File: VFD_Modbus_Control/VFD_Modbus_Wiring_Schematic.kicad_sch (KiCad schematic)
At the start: 11 parts

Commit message: Added the wiring to tie the grounds for the 5V PSU and the G540 PSU
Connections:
- net at Relay1. (NO): now also VFD1. (X6/Y1_FO)
- net at VFD1. (X6/Y1_FO): now also SPINDLE1. (RED); no longer Relay1. (NO)
- net at G1.10 (DISABLE_INPUT_(E-STOP)), G1.12 (POWER_SUPPLY_GND), PSU2. (+): now also PSU1. (+), Relay1. (NO), UC300ETH1. (DB25)
- new net: D1.1 (K), PSU1. (+), Relay1. (NO), UC300ETH1. (DB25)
- new net: Relay1. (NO), VFD1. (X6/Y1_FO)
- new net: RS485USB1. (+), VFD1. (X6/Y1_FO)
- new net: G1.7 (VFD_GROUND), PSU3. (L), SPINDLE1. (RED), VFD1. (X6/Y1_FO)
- new net: PSU3. (L), PUMP1. (L), VFD1. (X6/Y1_FO)
- new net: SPINDLE1. (RED), VFD1. (X6/Y1_FO) (x2)
- now unconnected: PSU1. (+), PSU1. (+)
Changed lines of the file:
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@@
+	)
+	(junction
+		(at 217.17 63.5)
+		(diameter 0)
+		(color 0 0 0 0)
 	)
 	(junction
@@
 	)
 	(junction
+		(at 217.17 49.53)
+		(diameter 0)
+		(color 0 0 0 0)
+	)
+	(junction
 		(at 227.33 52.07)
 		(diameter 0)
@@
 	(wire
 		(pts
-			(xy 200.66 49.53) (xy 270.51 49.53)
+			(xy 200.66 49.53) (xy 217.17 49.53)
 		)
 		(stroke
@@
 	(wire
 		(pts
+			(xy 217.17 49.53) (xy 217.17 63.5)
+		)
+		(stroke
+			(width 0)
+			(type default)
+		)
+	)
+	(wire
+		(pts
 			(xy 52.07 54.61) (xy 100.33 54.61)
 		)
@@
 		)
 		(stroke
+			(width 0)
+			(type default)
+		)
+	)
+	(wire
+		(pts
+			(xy 217.17 49.53) (xy 270.51 49.53)
+		)
+		(stroke

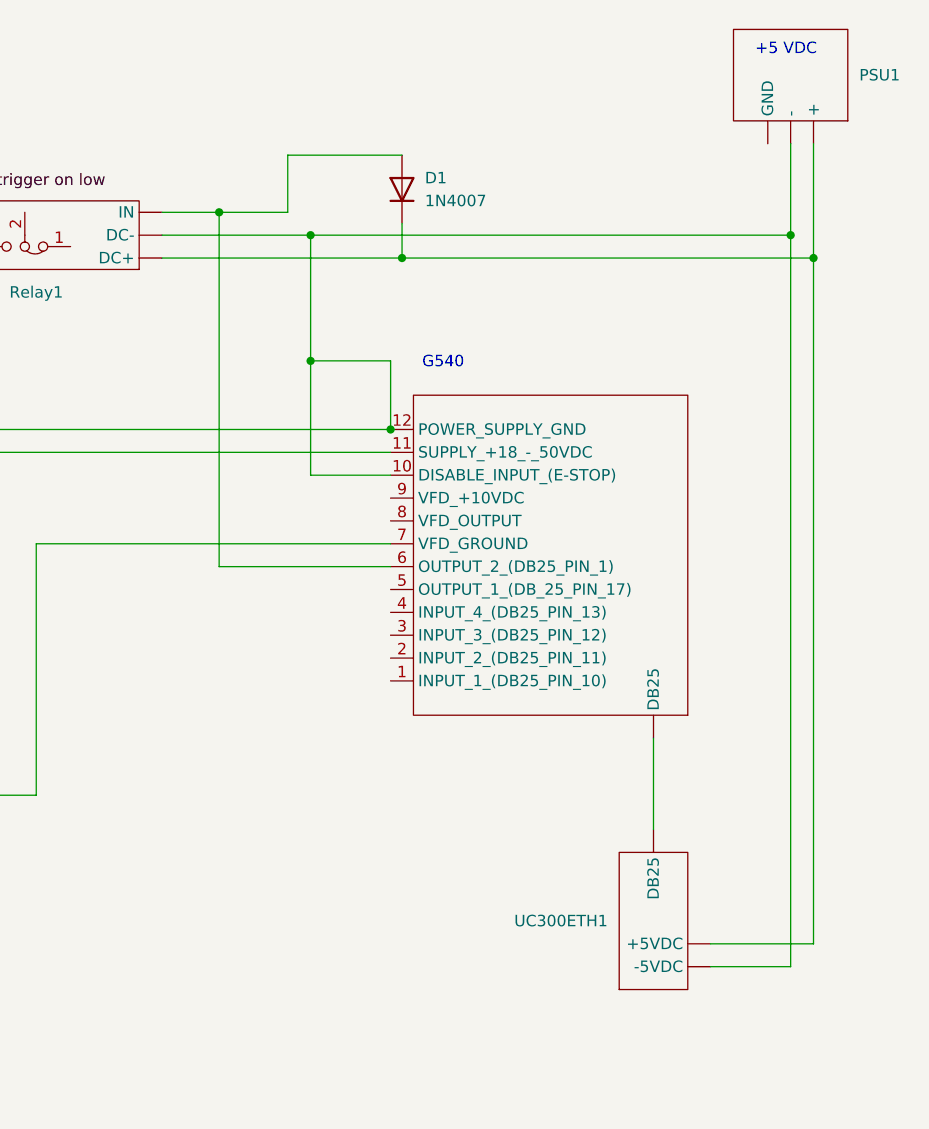
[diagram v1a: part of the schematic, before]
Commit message: Got voltage control working using two relays.
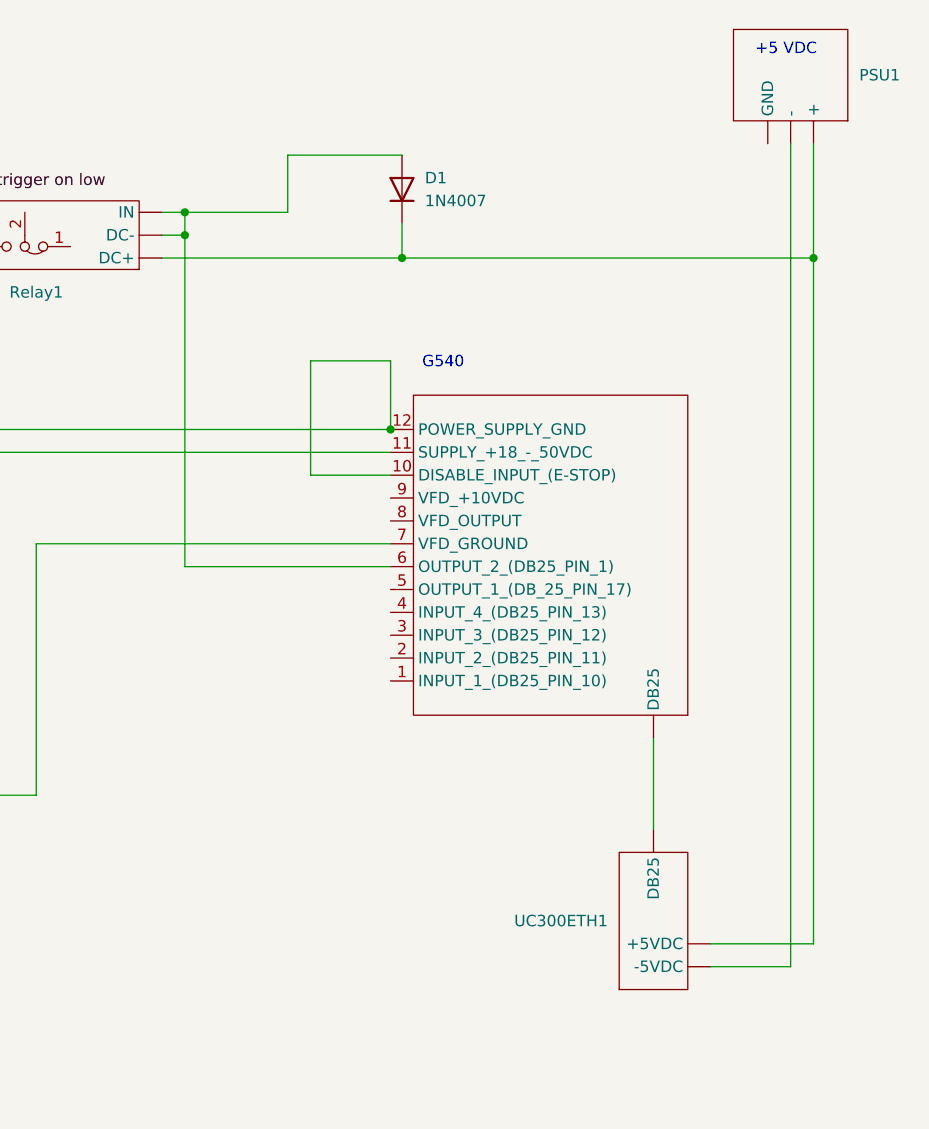
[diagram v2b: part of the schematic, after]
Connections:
- net at Relay1. (NO): now also VFD1. (X6/Y1_FO)
- net at VFD1. (X6/Y1_FO): now also SPINDLE1. (RED); no longer Relay1. (NO)
- new net: D1.1 (K), PSU1. (+), Relay1. (NO), UC300ETH1. (DB25)
- new net: Relay1. (NO), VFD1. (X6/Y1_FO)
- new net: RS485USB1. (+), VFD1. (X6/Y1_FO)
- new net: G1.10 (DISABLE_INPUT_(E-STOP)), G1.12 (POWER_SUPPLY_GND), PSU2. (+)
- new net: G1.7 (VFD_GROUND), PSU3. (L), SPINDLE1. (RED), VFD1. (X6/Y1_FO)
- new net: PSU3. (L), PUMP1. (L), VFD1. (X6/Y1_FO)
- new net: PSU1. (+), UC300ETH1. (DB25)
- new net: SPINDLE1. (RED), VFD1. (X6/Y1_FO) (x2)
- now unconnected: PSU1. (+), PSU1. (+), PSU2. (+)
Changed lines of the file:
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@@
-	)
-	(junction
-		(at 207.01 46.99)
-		(diameter 0)
-		(color 0 0 0 0)
-	)
-	(junction
-		(at 217.17 63.5)
-		(diameter 0)
-		(color 0 0 0 0)
 	)
 	(junction
@@
 	)
 	(junction
-		(at 270.51 49.53)
-		(diameter 0)
-		(color 0 0 0 0)
-	)
-	(junction
-		(at 217.17 49.53)
+		(at 203.2 49.53)
 		(diameter 0)
 		(color 0 0 0 0)
@@
 	)
 	(junction
+		(at 203.2 46.99)
+		(diameter 0)
+		(color 0 0 0 0)
+	)
+	(junction
 		(at 46.99 111.76)
 		(diameter 0)
@@
 	(wire
 		(pts
-			(xy 200.66 49.53) (xy 217.17 49.53)
-		)
-		(stroke
-			(width 0)
-			(type default)
-		)
-	)
-	(wire
-		(pts
 			(xy 20.32 143.51) (xy 95.25 143.51)
 		)
@@
 	(wire
 		(pts
-			(xy 270.51 39.37) (xy 270.51 49.53)
+			(xy 270.51 39.37) (xy 270.51 130.81)
 		)
 		(stroke
@@
 	(wire
 		(pts
-			(xy 217.17 49.53) (xy 217.17 63.5)
-		)
-		(stroke
-			(width 0)
-			(type default)
-		)
-	)
-	(wire
-		(pts
 			(xy 52.07 54.61) (xy 100.33 54.61)
 		)
@@
 	(wire
 		(pts
-			(xy 270.51 49.53) (xy 270.51 130.81)
-		)
-		(stroke
-			(width 0)
-			(type default)
-		)
-	)
-	(wire
-		(pts
 			(xy 78.74 39.37) (xy 78.74 46.99)
 		)
@@
 	(wire
 		(pts
-			(xy 217.17 49.53) (xy 270.51 49.53)
-		)
-		(stroke
-			(width 0)
-			(type default)
-		)
-	)
-	(wire
-		(pts
 			(xy 72.39 176.53) (xy 72.39 168.91)
 		)
@@
 	(wire
 		(pts
+			(xy 203.2 49.53) (xy 203.2 46.99)
+		)
+		(stroke
+			(width 0)
+			(type default)
+		)
+	)
+	(wire
+		(pts
+			(xy 203.2 46.99) (xy 200.66 46.99)
+		)
+		(stroke
+			(width 0)
+			(type default)
+		)
+	)
+	(wire
+		(pts
 			(xy 172.72 49.53) (xy 109.22 49.53)
 		)
@@
 	(wire
 		(pts
-			(xy 207.01 46.99) (xy 200.66 46.99)
-		)
-		(stroke
-			(width 0)
-			(type default)
-		)
-	)
-	(wire
-		(pts
 			(xy 102.87 143.51) (xy 102.87 53.34)
 		)
@@
 	(wire
 		(pts
+			(xy 200.66 49.53) (xy 203.2 49.53)
+		)
+		(stroke
+			(width 0)
+			(type default)
+		)
+	)
+	(wire
+		(pts
 			(xy 63.5 68.58) (xy 172.72 68.58)
 		)
@@
 	(wire
 		(pts
-			(xy 226.06 86.36) (xy 207.01 86.36)
+			(xy 226.06 86.36) (xy 203.2 86.36)
 		)
 		(stroke
@@
 	(wire
 		(pts
+			(xy 203.2 46.99) (xy 214.63 46.99)
+		)
+		(stroke
+			(width 0)
+			(type default)
+		)
+	)
+	(wire
+		(pts
 			(xy 226.06 76.2) (xy 217.17 76.2)
 		)
@@
 	(wire
 		(pts
-			(xy 207.01 86.36) (xy 207.01 46.99)
-		)
-		(stroke
-			(width 0)
-			(type default)
-		)
-	)
-	(wire
-		(pts
-			(xy 207.01 46.99) (xy 214.63 46.99)
-		)
-		(stroke
+			(xy 203.2 86.36) (xy 203.2 49.53)
+		)
+		(stroke
